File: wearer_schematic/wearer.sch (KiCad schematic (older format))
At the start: 46 parts

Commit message: add decoupling caps to esp
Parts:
- removed C?: 10uF, symbol Device:CP1
- added C?: 0.1uF, symbol Device:C_Small
- added C?: 10uF, symbol Device:C_Small
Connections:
- wire segments 106 -> 110
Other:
- moved on the sheet: R?, SW?, VR1
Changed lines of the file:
@@
-$EndComp
-$Comp
-L power:+3.3V #PWR?
-U 1 1 620D7784
-P 5900 2550
-F 0 "#PWR?" H 5900 2400 50  0001 C CNN
-F 1 "+3.3V" H 5915 2723 50  0000 C CNN
-F 2 "" H 5900 2550 50  0001 C CNN
-F 3 "" H 5900 2550 50  0001 C CNN
-	1    5900 2550
-	0    -1   -1   0
 $EndComp
 $Comp
@@
 Wire Wire Line
 	3050 4800 3150 4800
-$Comp
-L Noggin:S9V11F3S5C3 VR1
-U 1 1 621966CE
-P 2300 1650
-F 0 "VR1" V 1850 1550 50  0000 L CNN
-F 1 "S9V11F3S5C3" V 1950 1550 50  0000 L CNN
-F 2 "" H 2200 1100 50  0001 C CNN
-F 3 "" H 2200 1100 50  0001 C CNN
-	1    2300 1650
-	0    1    1    0
-$EndComp
-$Comp
-L Device:Battery_Cell BT?
-U 1 1 62197E53
-P 1150 2050
-F 0 "BT?" H 850 2200 50  0000 L CNN
-F 1 "Battery_Cell" H 550 2100 50  0000 L CNN
-F 2 "" V 1150 2110 50  0001 C CNN
-F 3 "~" V 1150 2110 50  0001 C CNN
-	1    1150 2050
-	1    0    0    -1
-$EndComp
-$Comp
-L power:+3.3V #PWR?
-U 1 1 6219FA43
-P 2000 900
-F 0 "#PWR?" H 2000 750 50  0001 C CNN
-F 1 "+3.3V" H 2015 1073 50  0000 C CNN
-F 2 "" H 2000 900 50  0001 C CNN
-F 3 "" H 2000 900 50  0001 C CNN
-	1    2000 900
-	1    0    0    -1
-$EndComp
-$Comp
-L power:GND #PWR?
-U 1 1 6219E17C
-P 2100 1500
-F 0 "#PWR?" H 2100 1250 50  0001 C CNN
-F 1 "GND" H 2105 1327 50  0000 C CNN
-F 2 "" H 2100 1500 50  0001 C CNN
-F 3 "" H 2100 1500 50  0001 C CNN
-	1    2100 1500
-	0    1    1    0
-$EndComp
-$Comp
-L power:GND #PWR?
-U 1 1 621B8E68
-P 1150 2150
-F 0 "#PWR?" H 1150 1900 50  0001 C CNN
-F 1 "GND" H 1155 1977 50  0000 C CNN
-F 2 "" H 1150 2150 50  0001 C CNN
-F 3 "" H 1150 2150 50  0001 C CNN
-	1    1150 2150
-	1    0    0    -1
-$EndComp
-Wire Wire Line
-	2100 1400 2000 1400
-$Comp
-L Switch:SW_SPST SW?
-U 1 1 621C2767
-P 1450 1600
-F 0 "SW?" H 1450 1835 50  0000 C CNN
-F 1 "SW_SPST" H 1450 1744 50  0000 C CNN
-F 2 "" H 1450 1600 50  0001 C CNN
-F 3 "~" H 1450 1600 50  0001 C CNN
-	1    1450 1600
-	1    0    0    -1
-$EndComp
-Wire Wire Line
-	1250 1600 1150 1600
-Wire Wire Line
-	1150 1600 1150 1850
-Wire Wire Line
-	6000 2550 5900 2550
 Wire Wire Line
 	3150 4800 3150 4700
@@
 L power:GND #PWR?
 U 1 1 621E738B
-P 6000 2450
-F 0 "#PWR?" H 6000 2200 50  0001 C CNN
-F 1 "GND" H 6005 2277 50  0000 C CNN
-F 2 "" H 6000 2450 50  0001 C CNN
-F 3 "" H 6000 2450 50  0001 C CNN
-	1    6000 2450
+P 5150 2350
+F 0 "#PWR?" H 5150 2100 50  0001 C CNN
+F 1 "GND" H 5155 2177 50  0000 C CNN
+F 2 "" H 5150 2350 50  0001 C CNN
+F 3 "" H 5150 2350 50  0001 C CNN
+	1    5150 2350
 	-1   0    0    1
 $EndComp
@@
 Wire Wire Line
 	2300 5500 2300 6050
-$Comp
-L Device:CP1 C?
-U 1 1 62221CB4
-P 2250 1000
-F 0 "C?" V 2502 1000 50  0000 C CNN
-F 1 "10uF" V 2411 1000 50  0000 C CNN
-F 2 "" H 2250 1000 50  0001 C CNN
-F 3 "~" H 2250 1000 50  0001 C CNN
-	1    2250 1000
-	0    -1   -1   0
-$EndComp
-Wire Wire Line
-	2000 900  2000 1000
-Wire Wire Line
-	2100 1000 2000 1000
-Connection ~ 2000 1000
-Wire Wire Line
-	2000 1000 2000 1400
 Text Notes 1550 5300 0    50   ~ 0
 Gas Sensor
-Text Notes 1300 1200 0    50   ~ 0
-Power
 $Comp
 L 74xx:74HC14 U?
@@
 Text GLabel 7400 2550 2    50   Input ~ 0
 SPI_MOSI
-Text Notes 2100 2150 0    50   ~ 0
-3.3V Step-Up Step-Down\nVoltage Regulator Module
 Text GLabel 9900 5500 0    50   Input ~ 0
 GPIO4
@@
 Text GLabel 6000 3250 0    50   Input ~ 0
 ADC1_CH5
-$Comp
-L Device:R R?
-U 1 1 6223F31D
-P 1750 2200
-F 0 "R?" H 1820 2246 50  0000 L CNN
-F 1 "22k" H 1820 2155 50  0000 L CNN
-F 2 "" V 1680 2200 50  0001 C CNN
-F 3 "~" H 1750 2200 50  0001 C CNN
-	1    1750 2200
-	-1   0    0    1
-$EndComp
-$Comp
-L Device:R R?
-U 1 1 62242505
-P 1750 2700
-F 0 "R?" H 1820 2746 50  0000 L CNN
-F 1 "68k" H 1820 2655 50  0000 L CNN
-F 2 "" V 1680 2700 50  0001 C CNN
-F 3 "~" H 1750 2700 50  0001 C CNN
-	1    1750 2700
-	-1   0    0    1
-$EndComp
-$Comp
-L power:GND #PWR?
-U 1 1 62242CEE
-P 1750 2850
-F 0 "#PWR?" H 1750 2600 50  0001 C CNN
-F 1 "GND" H 1755 2677 50  0000 C CNN
-F 2 "" H 1750 2850 50  0001 C CNN
-F 3 "" H 1750 2850 50  0001 C CNN
-	1    1750 2850
-	1    0    0    -1
-$EndComp
-Wire Wire Line
-	1750 2350 1750 2450
-Wire Wire Line
-	1750 2450 1800 2450
-Connection ~ 1750 2450
-Wire Wire Line
-	1750 2450 1750 2550
-Text GLabel 1800 2450 2    50   Input ~ 0
-ADC1_CH6
-Wire Wire Line
-	1650 1600 1750 1600
-Wire Wire Line
-	1750 1600 1750 2050
-Connection ~ 1750 1600
-Wire Wire Line
-	1750 1600 2100 1600
 Text Notes 950  3350 0    50   ~ 0
 5V Power
@@
 	0    1    1    0
 $EndComp
-Text Notes 1900 2700 0    50   ~ 0
-Battery\nMonitoring
 Text GLabel 6000 3450 0    50   Input ~ 0
 GPIO26
@@
 Text GLabel 7400 3150 2    50   Input ~ 0
 GPIO17
-$Comp
-L power:GND #PWR?
-U 1 1 622272CD
-P 2400 1000
-F 0 "#PWR?" H 2400 750 50  0001 C CNN
-F 1 "GND" H 2405 827 50  0000 C CNN
-F 2 "" H 2400 1000 50  0001 C CNN
-F 3 "" H 2400 1000 50  0001 C CNN
-	1    2400 1000
-	0    -1   -1   0
-$EndComp
 Text GLabel 8500 1100 0    50   Input ~ 0
 SDO
@@
 Text Notes 7850 2500 0    50   ~ 0
 (unsure)
+$Comp
+L Noggin:S9V11F3S5C3 VR1
+U 1 1 621966CE
+P 2300 1500
+F 0 "VR1" V 1850 1400 50  0000 L CNN
+F 1 "S9V11F3S5C3" V 1950 1400 50  0000 L CNN
+F 2 "" H 2200 950 50  0001 C CNN
+F 3 "" H 2200 950 50  0001 C CNN
+	1    2300 1500
+	0    1    1    0
+$EndComp
+$Comp
+L Device:Battery_Cell BT?
+U 1 1 62197E53
+P 1150 1900
+F 0 "BT?" H 850 2050 50  0000 L CNN
+F 1 "Battery_Cell" H 550 1950 50  0000 L CNN
+F 2 "" V 1150 1960 50  0001 C CNN
+F 3 "~" V 1150 1960 50  0001 C CNN
+	1    1150 1900
+	1    0    0    -1
+$EndComp
+$Comp
+L power:+3.3V #PWR?
+U 1 1 6219FA43
+P 2000 1150
+F 0 "#PWR?" H 2000 1000 50  0001 C CNN
+F 1 "+3.3V" H 2015 1323 50  0000 C CNN
+F 2 "" H 2000 1150 50  0001 C CNN
+F 3 "" H 2000 1150 50  0001 C CNN
+	1    2000 1150
+	1    0    0    -1
+$EndComp
+$Comp
+L power:GND #PWR?
+U 1 1 6219E17C
+P 2100 1350
+F 0 "#PWR?" H 2100 1100 50  0001 C CNN
+F 1 "GND" H 2105 1177 50  0000 C CNN
+F 2 "" H 2100 1350 50  0001 C CNN
+F 3 "" H 2100 1350 50  0001 C CNN
+	1    2100 1350
+	0    1    1    0
+$EndComp
+$Comp
+L power:GND #PWR?
+U 1 1 621B8E68
+P 1150 2000
+F 0 "#PWR?" H 1150 1750 50  0001 C CNN
+F 1 "GND" H 1155 1827 50  0000 C CNN
+F 2 "" H 1150 2000 50  0001 C CNN
+F 3 "" H 1150 2000 50  0001 C CNN
+	1    1150 2000
+	1    0    0    -1
+$EndComp
+Wire Wire Line
+	2100 1250 2000 1250
+$Comp
+L Switch:SW_SPST SW?
+U 1 1 621C2767
+P 1450 1450
+F 0 "SW?" H 1450 1685 50  0000 C CNN
+F 1 "SW_SPST" H 1450 1594 50  0000 C CNN
+F 2 "" H 1450 1450 50  0001 C CNN
+F 3 "~" H 1450 1450 50  0001 C CNN
+	1    1450 1450
+	1    0    0    -1
+$EndComp
+Wire Wire Line
+	1250 1450 1150 1450
+Wire Wire Line
+	1150 1450 1150 1700
+Text Notes 1300 1050 0    50   ~ 0
+Power
+Text Notes 2100 2000 0    50   ~ 0
+3.3V Step-Up Step-Down\nVoltage Regulator Module
+$Comp
+L Device:R R?
+U 1 1 6223F31D
+P 1750 2050
+F 0 "R?" H 1820 2096 50  0000 L CNN
+F 1 "22k" H 1820 2005 50  0000 L CNN
+F 2 "" V 1680 2050 50  0001 C CNN
+F 3 "~" H 1750 2050 50  0001 C CNN
+	1    1750 2050
+	-1   0    0    1
+$EndComp
+$Comp
+L Device:R R?
+U 1 1 62242505
+P 1750 2550
+F 0 "R?" H 1820 2596 50  0000 L CNN
+F 1 "68k" H 1820 2505 50  0000 L CNN
+F 2 "" V 1680 2550 50  0001 C CNN
+F 3 "~" H 1750 2550 50  0001 C CNN
+	1    1750 2550
+	-1   0    0    1
+$EndComp
+$Comp
+L power:GND #PWR?
+U 1 1 62242CEE
+P 1750 2700
+F 0 "#PWR?" H 1750 2450 50  0001 C CNN
+F 1 "GND" H 1755 2527 50  0000 C CNN
+F 2 "" H 1750 2700 50  0001 C CNN
+F 3 "" H 1750 2700 50  0001 C CNN
+	1    1750 2700
+	1    0    0    -1
+$EndComp
+Wire Wire Line
+	1750 2200 1750 2300
+Wire Wire Line
+	1750 2300 1800 2300
+Connection ~ 1750 2300
+Wire Wire Line
+	1750 2300 1750 2400
+Text GLabel 1800 2300 2    50   Input ~ 0
+ADC1_CH6
+Wire Wire Line
+	1650 1450 1750 1450
+Wire Wire Line
+	1750 1450 1750 1900
+Connection ~ 1750 1450
+Wire Wire Line
+	1750 1450 2100 1450
+Text Notes 1900 2550 0    50   ~ 0
+Battery\nMonitoring
+Wire Wire Line
+	2000 1150 2000 1250
+$Comp
+L power:+3.3V #PWR?
+U 1 1 620D7784
+P 5150 2550
+F 0 "#PWR?" H 5150 2400 50  0001 C CNN
+F 1 "+3.3V" H 5165 2723 50  0000 C CNN
+F 2 "" H 5150 2550 50  0001 C CNN
+F 3 "" H 5150 2550 50  0001 C CNN
+	1    5150 2550
+	-1   0    0    1
+$EndComp
+$Comp
+L Device:C_Small C?
+U 1 1 621E55A2
+P 5650 2450
+F 0 "C?" H 5742 2496 50  0000 L CNN
+F 1 "0.1uF" H 5742 2405 50  0000 L CNN
+F 2 "" H 5650 2450 50  0001 C CNN
+F 3 "~" H 5650 2450 50  0001 C CNN
+	1    5650 2450
+	1    0    0    -1
+$EndComp
+$Comp
+L Device:C_Small C?
+U 1 1 621F0155
+P 5300 2450
+F 0 "C?" H 5392 2496 50  0000 L CNN
+F 1 "10uF" H 5392 2405 50  0000 L CNN
+F 2 "" H 5300 2450 50  0001 C CNN
+F 3 "~" H 5300 2450 50  0001 C CNN
+	1    5300 2450
+	1    0    0    -1
+$EndComp
+Wire Wire Line
+	5650 2550 6000 2550
+Wire Wire Line
+	5300 2550 5150 2550
+Wire Wire Line
+	5300 2550 5650 2550
+Connection ~ 5300 2550
+Connection ~ 5650 2550
+Wire Wire Line
+	6000 2450 6000 2350
+Wire Wire Line
+	6000 2350 5650 2350
+Wire Wire Line
+	5650 2350 5300 2350
+Connection ~ 5650 2350
+Wire Wire Line
+	5300 2350 5150 2350
+Connection ~ 5300 2350
 $EndSCHEMATC

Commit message: added footprints
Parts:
- removed C?: 1uF, symbol Device:CP1
- added C?: 1uF, symbol Device:C_Small
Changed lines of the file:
@@
-$EndComp
-$Comp
-L Device:CP1 C?
-U 1 1 62270C52
-P 4150 1750
-F 0 "C?" V 4402 1750 50  0000 C CNN
-F 1 "1uF" V 4311 1750 50  0000 C CNN
-F 2 "" H 4150 1750 50  0001 C CNN
-F 3 "~" H 4150 1750 50  0001 C CNN
-	1    4150 1750
-	1    0    0    -1
 $EndComp
 $Comp
@@
 Wire Wire Line
 	3950 2050 3950 2100
-Wire Wire Line
-	4150 1900 4150 2050
 Wire Wire Line
 	4150 2050 3950 2050
@@
 	5300 2350 5150 2350
 Connection ~ 5300 2350
+$Comp
+L Device:C_Small C?
+U 1 1 6221322F
+P 4150 1700
+F 0 "C?" H 4242 1746 50  0000 L CNN
+F 1 "1uF" H 4242 1655 50  0000 L CNN
+F 2 "" H 4150 1700 50  0001 C CNN
+F 3 "~" H 4150 1700 50  0001 C CNN
+	1    4150 1700
+	1    0    0    -1
+$EndComp
+Wire Wire Line
+	4150 1800 4150 2050
 $EndSCHEMATC

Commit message: started footprint
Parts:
- removed BT?: Battery_Cell, symbol Device:Battery_Cell
- removed C? (x2): 0.1uF, symbol Device:CP1
- removed SW? (x2): SW_SPST, symbol Switch:SW_SPST
- added C2, C3: 0.1uF, Capacitor_SMD:C_0805_2012Metric_Pad1.15x1.40mm_HandSolder, symbol Device:C_Small
- added C7: 100 nF, Capacitor_SMD:C_0805_2012Metric_Pad1.15x1.40mm_HandSolder, symbol Device:C_Small
- added J1: Conn_01x02_Male, Connector_PinHeader_2.54mm:PinHeader_1x02_P2.54mm_Vertical, symbol Connector:Conn_01x02_Male
- added SW1: SW_SPST, Connector_PinHeader_2.54mm:PinHeader_1x02_P2.54mm_Vertical, symbol Switch:SW_SPST
- added SW2: SW_Push, symbol Switch:SW_Push
- C1, C4, C5, C6, C8: renamed from C?; footprint (none) -> Capacitor_SMD:C_0805_2012Metric_Pad1.15x1.40mm_HandSolder
- D1, D2: renamed from D?; footprint (none) -> LED_SMD:LED_1206_3216Metric_Pad1.42x1.75mm_HandSolder
- J2: renamed from J?; footprint (none) -> Connector_PinHeader_2.54mm:PinHeader_1x06_P2.54mm_Vertical
- LS1: renamed from LS?; footprint PS1240P02BT -> noggin:PS1240P02BT
- Q1: renamed from Q?; footprint SOT95P280X125-3N -> noggin:SOT95P280X125-3N
- R1, R10, R11, R12, R13, R14, R15, R16, R2, R3, R4, R5, R6, R7, R8, R9: renamed from R?; footprint (none) -> Resistor_SMD:R_0805_2012Metric_Pad1.15x1.40mm_HandSolder
- SW3, SW4: renamed from SW?; footprint (none) -> Connector_PinHeader_2.54mm:PinHeader_1x02_P2.54mm_Vertical
- U1: renamed from U?; footprint (none) -> noggin:MQ-9B
- U2: renamed from U?; footprint (none) -> Package_DIP:DIP-14_W7.62mm
- U3: renamed from ANT?; footprint ESP32WROOM32D -> noggin:ESP32WROOM32D
- U4: renamed from U?; footprint QFN_6DSLTR_STM -> noggin:LSM6DSLTR
- gave numbers to parts that had none: 2
- renumbered VR2 to VR1, VR1 to VR2
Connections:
- wire segments 110 -> 111
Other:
- moved on the sheet: LS1, R7

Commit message: edit pcb
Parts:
- added R5: 36, Resistor_SMD:R_0805_2012Metric_Pad1.15x1.40mm_HandSolder, symbol Device:R
- D1, D2: footprint LED_SMD:LED_1206_3216Metric_Pad1.42x1.75mm_HandSolder -> LED_SMD:LED_0805_2012Metric_Pad1.15x1.40mm_HandSolder
- R12: renamed from R11; value R -> 68
- R15: renamed from R14; value R -> 68
- R4: value 71.167 -> 36
- SW2: footprint (none) -> Button_Switch_THT:SW_PUSH_6mm
- U5: footprint (none) -> Connector_PinHeader_2.54mm:PinHeader_1x03_P2.54mm_Horizontal
- U6: footprint (none) -> noggin:RFM9x
- VR1: footprint (none) -> Connector_PinHeader_2.54mm:PinHeader_1x03_P2.54mm_Vertical
- VR2: footprint (none) -> Connector_PinHeader_2.54mm:PinHeader_1x06_P2.54mm_Vertical
- renumbered R9 to R10, R10 to R11, R12 to R13, R13 to R14, R15 to R16, R16 to R17, R5 to R6, R6 to R7, R7 to R8, R8 to R9
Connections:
- net +3V3: now also VR2.5 (VOUT)
- net GND: now also VR2.4 (GND), R5.2; no longer R4.2
- net at VR2.3 (VIN): now also R2.2, SW1.2 (B)
- new net: R4.2, R5.1
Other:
- note added: "3.3V Step-Up Step-Down\nVoltage Regulator"
- note added: "5V Step-Up\nVoltage Regulator"
- note added: "Accelerometer"
- note added: "Programming Header"
- note removed: "(unsure)"
- note removed: "3.3V Step-Up Step-Down\nVoltage Regulator Module"
- note removed: "5V Step-Up\nVoltage Regulator Module"
- note removed: "ESPFlasher Programming Header"
- moved on the sheet: C1, C2, C3, D1, D2, J2, LS1, Q1, R1, R10, R11, R12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

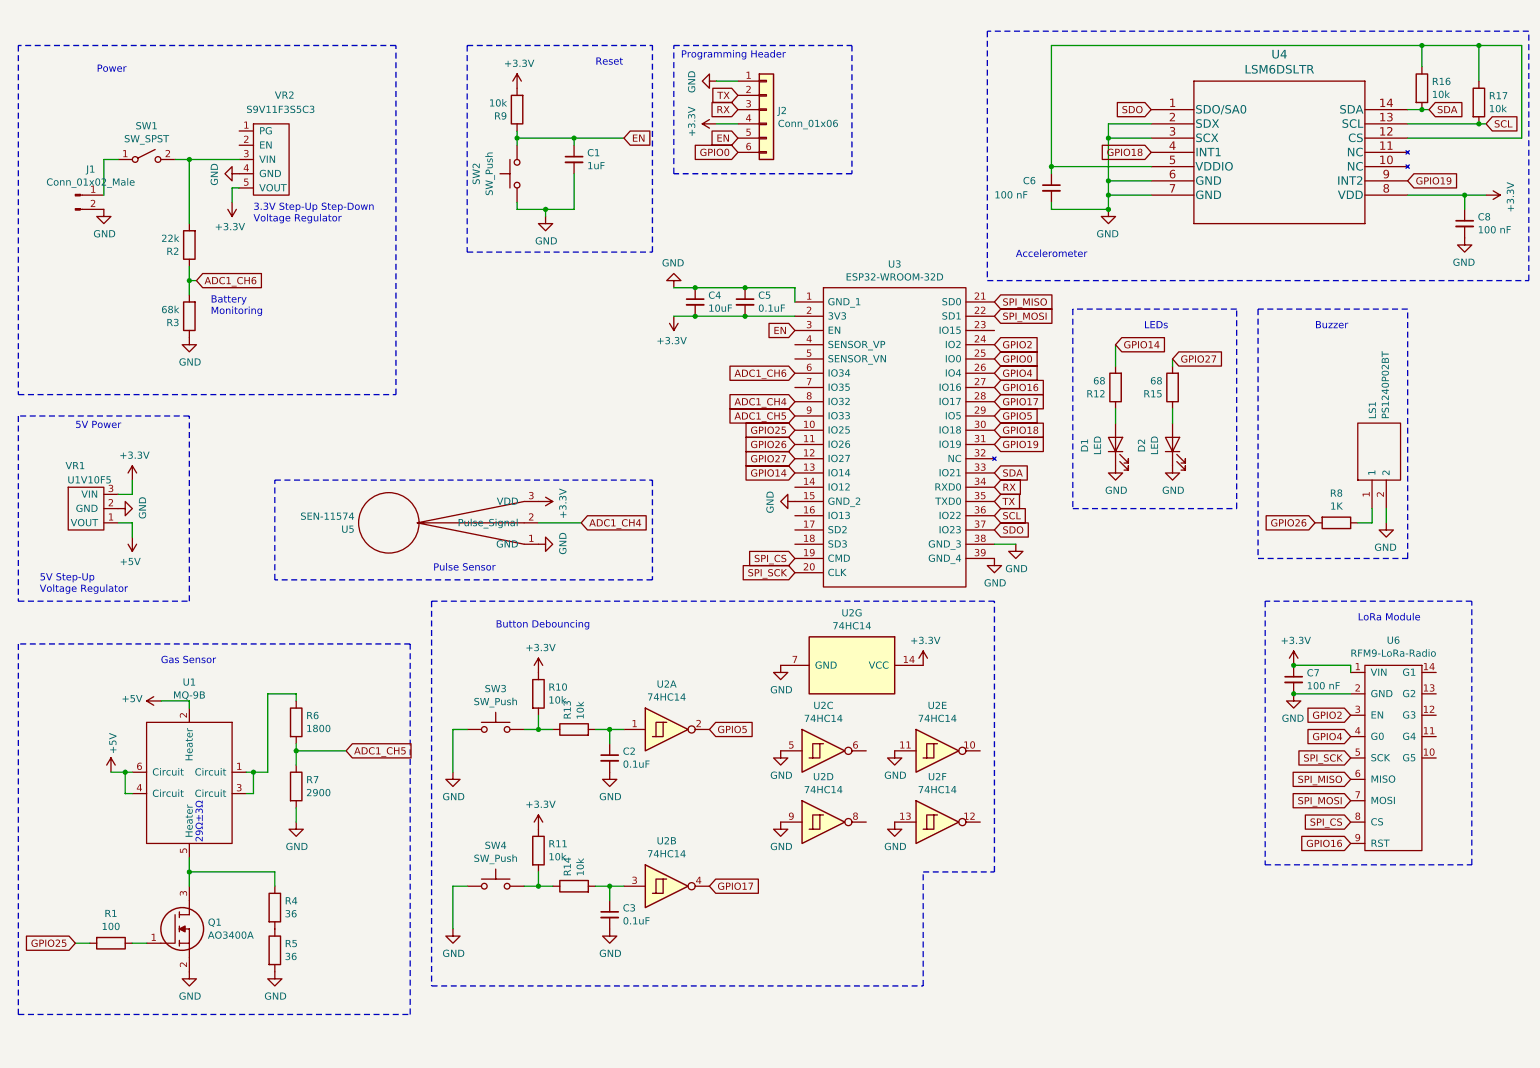
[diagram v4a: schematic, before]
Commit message: arranging components
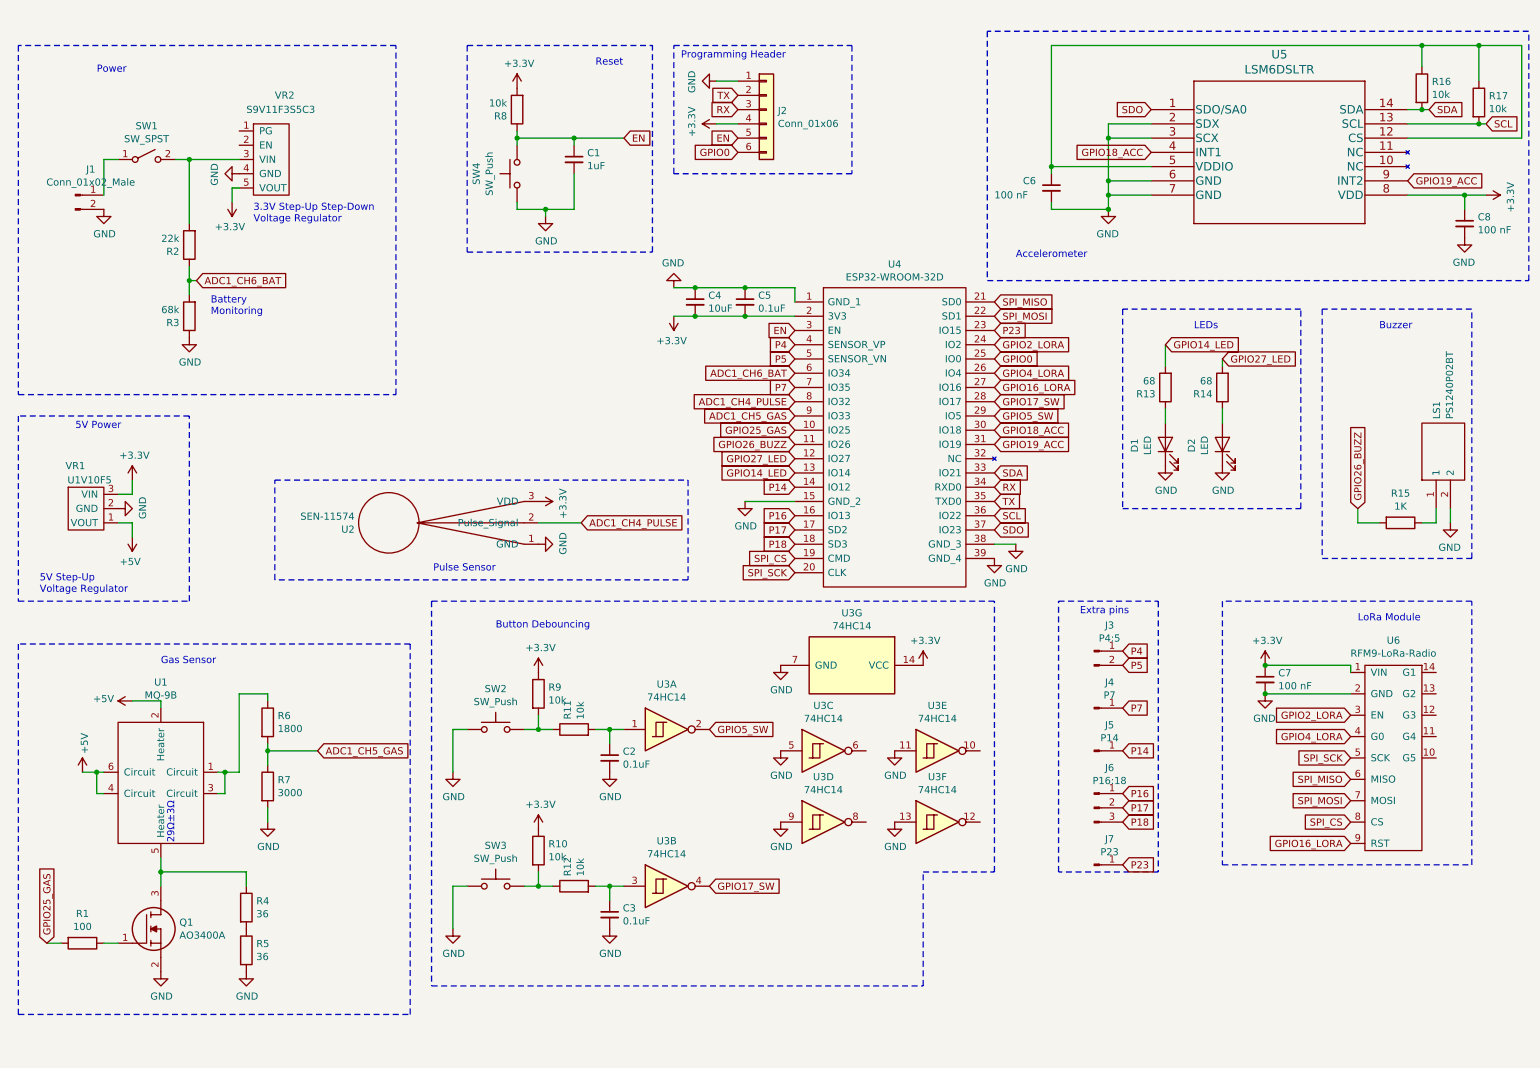
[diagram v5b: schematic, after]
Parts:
- added J3: P4:5, Connector_PinHeader_2.54mm:PinHeader_1x02_P2.54mm_Vertical, symbol Connector:Conn_01x02_Male
- added J4: P7, Connector_PinHeader_2.54mm:PinHeader_1x01_P2.54mm_Vertical, symbol Connector:Conn_01x01_Male
- added J5: P14, Connector_PinHeader_2.54mm:PinHeader_1x01_P2.54mm_Vertical, symbol Connector:Conn_01x01_Male
- added J6: P16:18, Connector_PinHeader_2.54mm:PinHeader_1x03_P2.54mm_Vertical, symbol Connector:Conn_01x03_Male
- added J7: P23, Connector_PinHeader_2.54mm:PinHeader_1x01_P2.54mm_Vertical, symbol Connector:Conn_01x01_Male
- R7: value 2900 -> 3000
- VR1: footprint Connector_PinHeader_2.54mm:PinHeader_1x03_P2.54mm_Vertical -> noggin:U1V10F5-VR
- VR2: footprint Connector_PinHeader_2.54mm:PinHeader_1x06_P2.54mm_Vertical -> noggin:S9V11F3S5C3
- renumbered R11 to R10, R13 to R11, R14 to R12, R12 to R13, R15 to R14, R8 to R15, R9 to R8, R10 to R9, SW3 to SW2, SW4 to SW3, SW2 to SW4, U5 to U2, U2 to U3, U3 to U4, U4 to U5
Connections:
- net P14: now reaches U4.14 (IO12)
- net P14: now also J5.1 (Pin_1)
- net P16: now reaches U4.16 (IO13)
- net P16: now also J6.1 (Pin_1)
- net P17: now reaches U4.17 (SD2)
- net P17: now also J6.2 (Pin_2)
- net P18: now reaches U4.18 (SD3)
- net P18: now also J6.3 (Pin_3)
- net P23: now reaches U4.23 (IO15)
- net P23: now also J7.1 (Pin_1)
- net P4: now reaches U4.4 (SENSOR_VP)
- net P4: now also J3.1 (Pin_1)
- net P5: now reaches U4.5 (SENSOR_VN)
- net P5: now also J3.2 (Pin_2)
- net P7: now reaches U4.7 (IO35)
- net P7: now also J4.1 (Pin_1)
- net ADC1_CH4 renamed ADC1_CH4_PULSE
- net ADC1_CH5 renamed ADC1_CH5_GAS
- net ADC1_CH6 renamed ADC1_CH6_BAT
- net GPIO14 renamed GPIO14_LED
- net GPIO16 renamed GPIO16_LORA
- net GPIO17 renamed GPIO17_SW
- net GPIO18 renamed GPIO18_ACC
- net GPIO19 renamed GPIO19_ACC
- net GPIO2 renamed GPIO2_LORA
- net GPIO25 renamed GPIO25_GAS
- net GPIO26 renamed GPIO26_BUZZ
- net GPIO27 renamed GPIO27_LED
- net GPIO4 renamed GPIO4_LORA
- net GPIO5 renamed GPIO5_SW
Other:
- note added: "Extra pins"
- moved on the sheet: C7, D1, D2, LS1, Q1, R1, R13, R14, R15, R4, R5, R6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
